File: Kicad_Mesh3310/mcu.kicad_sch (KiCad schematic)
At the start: 41 parts, among them U13 NRF52840-QIAA-R, U4 MX25R1635FZNIH0, X2 S201632M10PF10PPM 32MHz, X4 32.768KHz

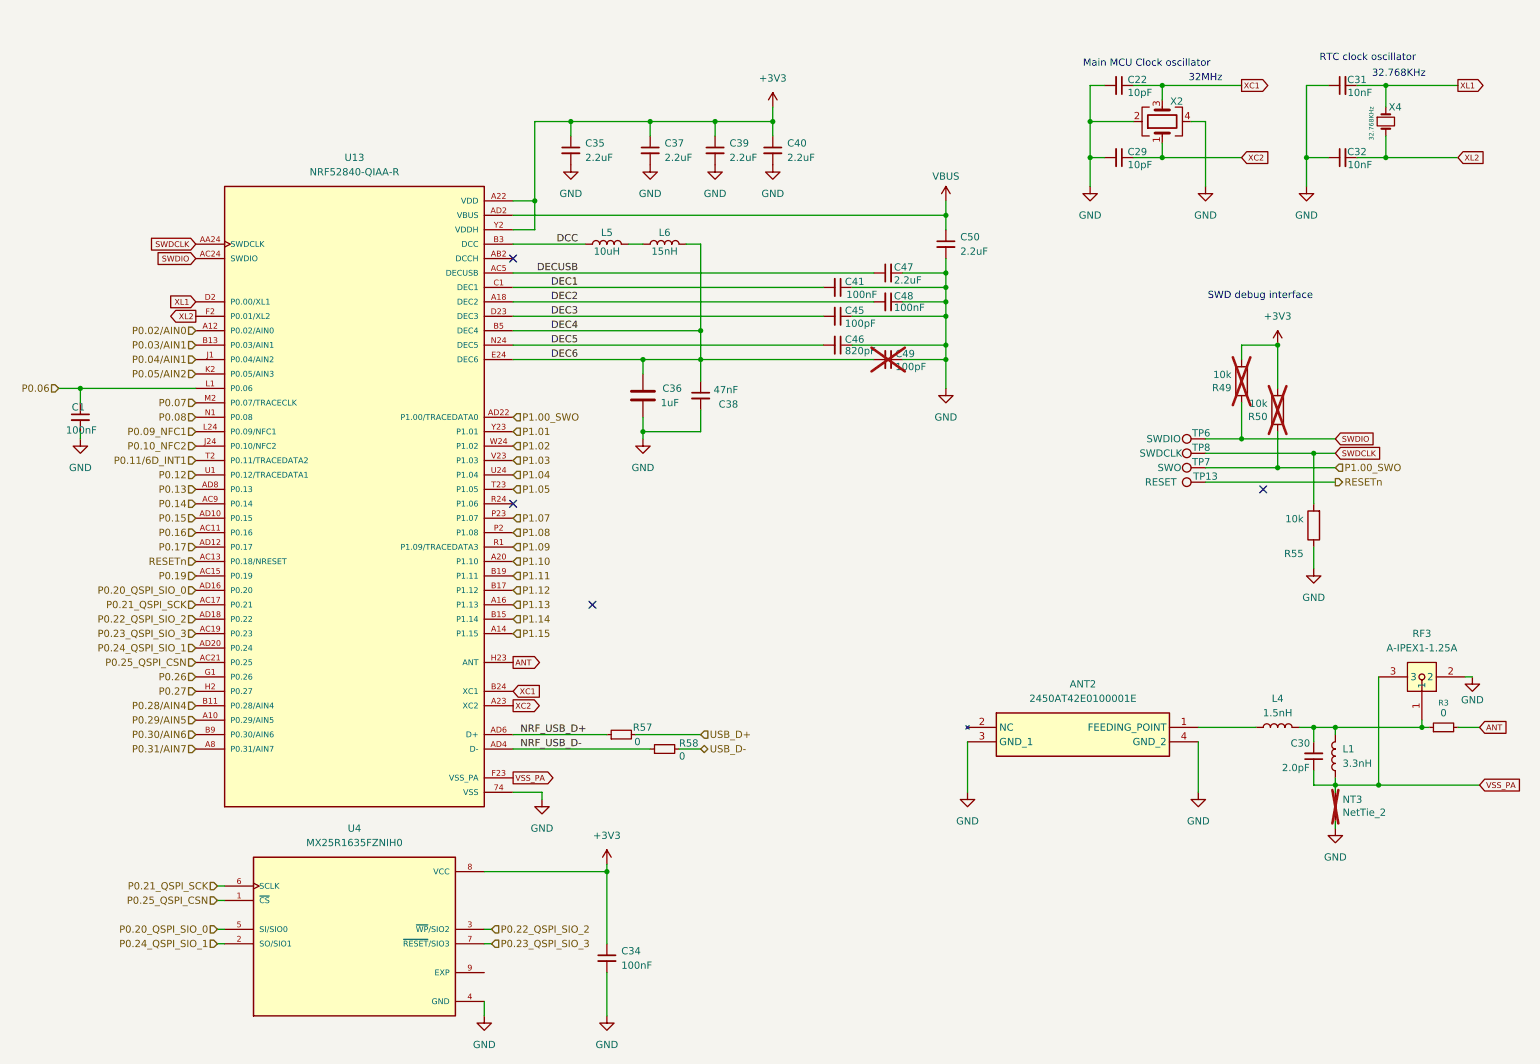
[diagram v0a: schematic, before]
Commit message: shematic changes
small changes in NRF component
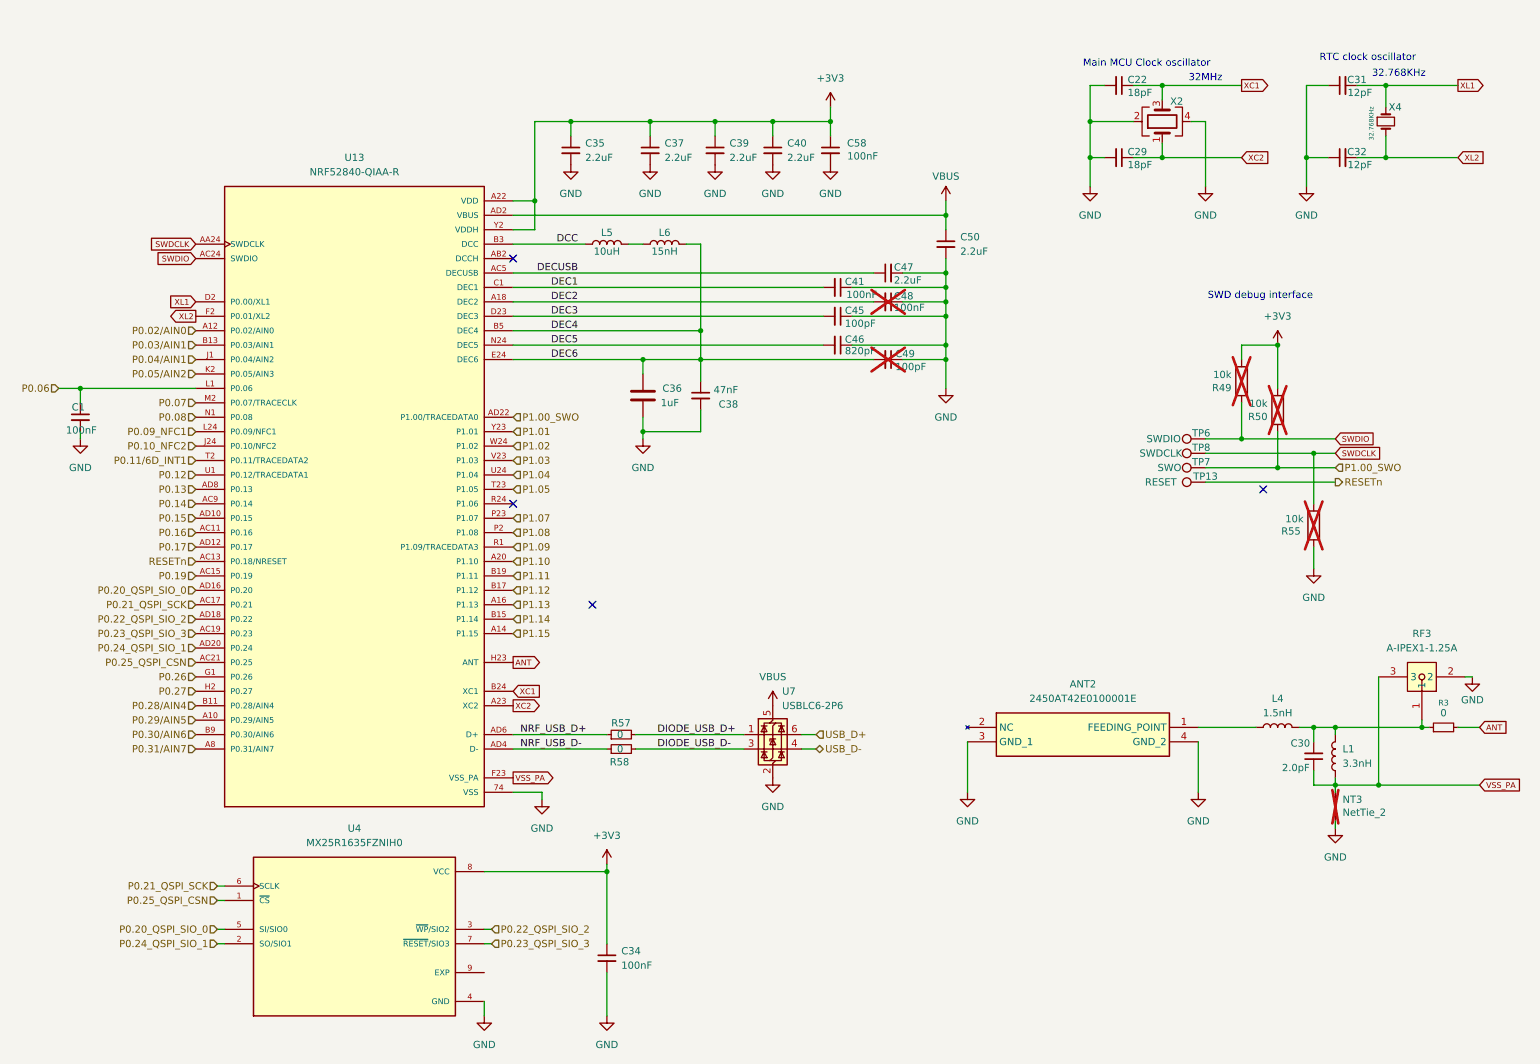
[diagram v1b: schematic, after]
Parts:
- added C58: 100nF, Capacitor_SMD:C_0402_1005Metric, symbol Device:C_Small
- added U7: USBLC6-2P6, Package_TO_SOT_SMD:SOT-666, symbol Power_Protection:USBLC6-2P6
- C22, C29: value 10pF -> 18pF
- C31, C32: value 10nF -> 12pF
- C48, R55: now not fitted
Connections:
- net +3V3: now also C58.1
- net GND: now also C58.2, U7.2 (GND)
- net USB_D+: now also U7.6 (I/O1); no longer R57.2
- net USB_D-: now also U7.4 (I/O2); no longer R58.2
- net VBUS: now also U7.5 (VBUS)
- new net DIODE_USB_D+: R57.2, U7.1 (I/O1)
- new net DIODE_USB_D-: R58.2, U7.3 (I/O2)
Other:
- moved on the sheet: R58

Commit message: Schematic changes
Adding gsm module , interfaces : mic+earspeaker
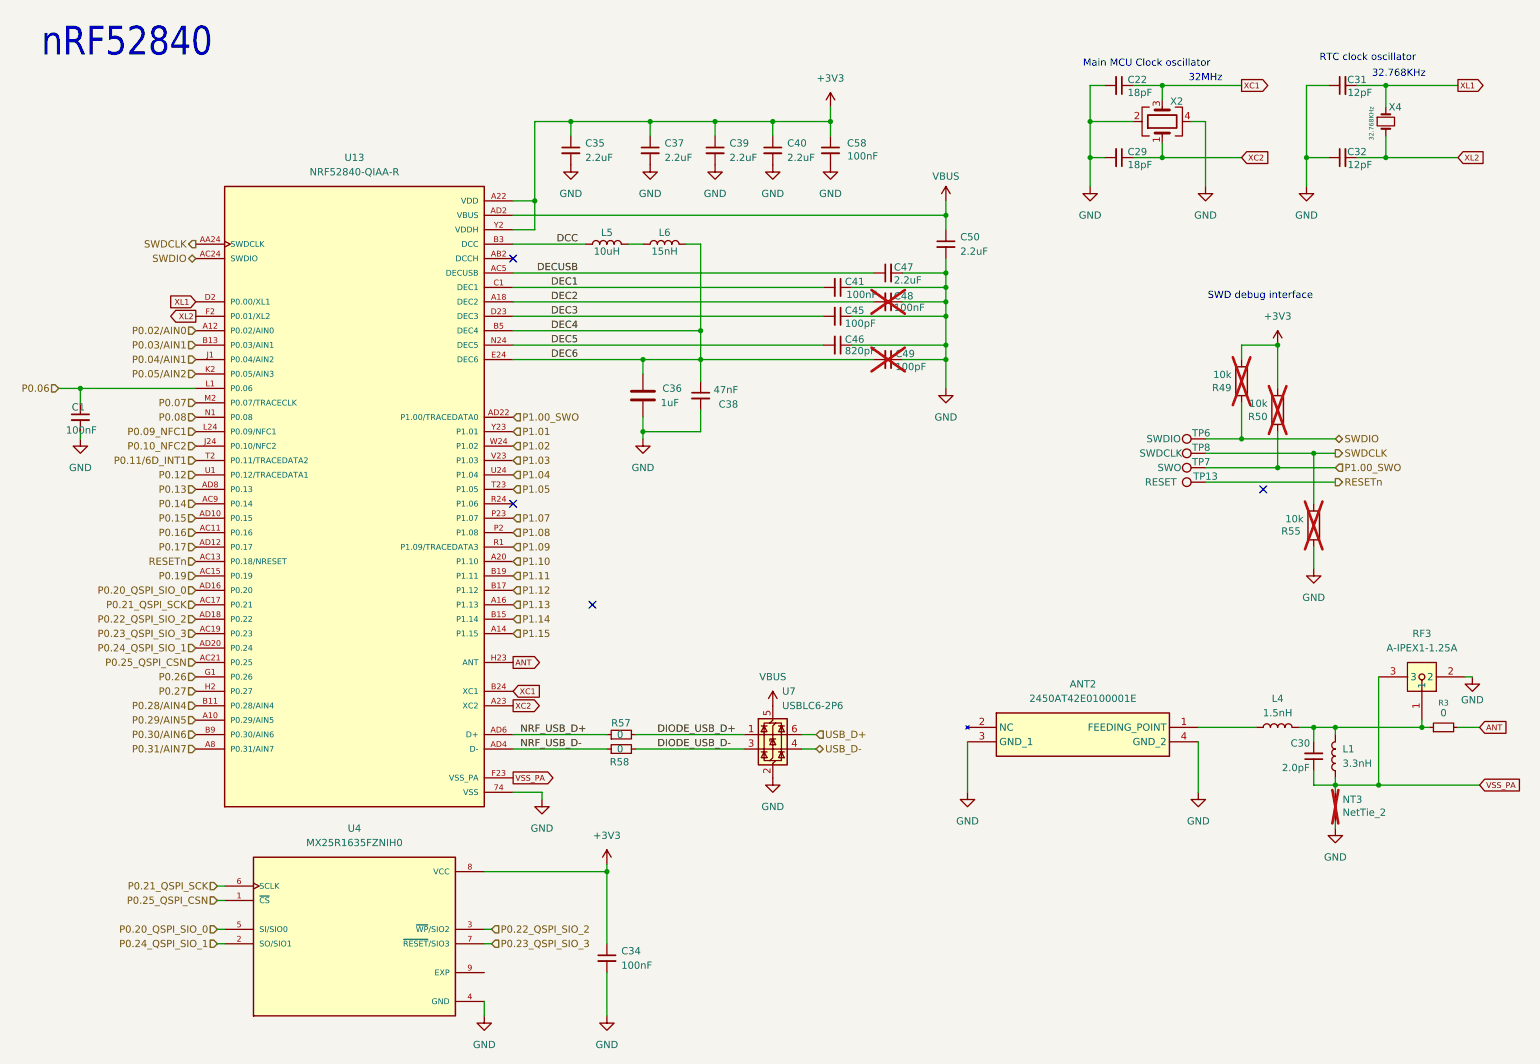
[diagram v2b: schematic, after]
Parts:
- C1: footprint Capacitor_SMD:C_0201_0603Metric -> Resistor_SMD:R_0201_0603Metric
- C58: footprint Capacitor_SMD:C_0402_1005Metric -> Capacitor_SMD:C_0201_0603Metric
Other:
- note added: "nRF52840"
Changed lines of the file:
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@@
 		)
 	)
+	(text "nRF52840"
+		(exclude_from_sim no)
+		(at 18.542 22.098 0)
+		(effects
+			(font
+				(size 5.08 4.318)
+			)
+			(justify left bottom)
+		)
+	)
 	(text "32MHz"
 		(exclude_from_sim no)
@@
 		)
 	)
-	(global_label "SWDCLK"
-		(shape input)
-		(at 246.38 91.44 0)
-		(fields_autoplaced yes)
-		(effects
-			(font
-				(size 1.016 1.016)
-			)
-			(justify left)
-		)
-		(property "Intersheetrefs" "${INTERSHEET_REFS}"
-			(at 254.7671 91.44 0)
-			(effects
-				(font
-					(size 1.27 1.27)
-				)
-				(justify left)
-				(hide yes)
-			)
-		)
-	)
-	(global_label "SWDIO"
-		(shape input)
-		(at 45.72 57.15 180)
-		(fields_autoplaced yes)
-		(effects
-			(font
-				(size 1.016 1.016)
-			)
-			(justify right)
-		)
-		(property "Intersheetrefs" "${INTERSHEET_REFS}"
-			(at 38.6392 57.15 0)
-			(effects
-				(font
-					(size 1.27 1.27)
-				)
-				(justify right)
-				(hide yes)
-			)
-		)
-	)
 	(global_label "XL1"
 		(shape output)
@@
 		)
 	)
-	(global_label "SWDCLK"
-		(shape input)
-		(at 45.72 54.61 180)
-		(fields_autoplaced yes)
-		(effects
-			(font
-				(size 1.016 1.016)
-			)
-			(justify right)
-		)
-		(property "Intersheetrefs" "${INTERSHEET_REFS}"
-			(at 37.3329 54.61 0)
-			(effects
-				(font
-					(size 1.27 1.27)
-				)
-				(justify right)
-				(hide yes)
-			)
-		)
-	)
 	(global_label "XC2"
 		(shape input)
@@
 		)
 	)
-	(global_label "SWDIO"
-		(shape input)
-		(at 246.38 88.9 0)
-		(fields_autoplaced yes)
-		(effects
-			(font
-				(size 1.016 1.016)
-			)
-			(justify left)
-		)
-		(property "Intersheetrefs" "${INTERSHEET_REFS}"
-			(at 253.4608 88.9 0)
-			(effects
-				(font
-					(size 1.27 1.27)
-				)
-				(justify left)
-				(hide yes)
-			)
-		)
-	)
 	(hierarchical_label "P1.07"
 		(shape input)
@@
 		)
 	)
+	(hierarchical_label "SWDIO"
+		(shape bidirectional)
+		(at 246.38 88.9 0)
+		(effects
+			(font
+				(size 1.27 1.27)
+			)
+			(justify left)
+		)
+	)
 	(hierarchical_label "P0.07"
 		(shape input)
@@
 		)
 	)
+	(hierarchical_label "SWDIO"
+		(shape bidirectional)
+		(at 45.72 57.15 180)
+		(effects
+			(font
+				(size 1.27 1.27)
+			)
+			(justify right)
+		)
+	)
 	(hierarchical_label "P1.00_SWO"
 		(shape input)
@@
 		)
 	)
+	(hierarchical_label "SWDCLK"
+		(shape output)
+		(at 45.72 54.61 180)
+		(effects
+			(font
+				(size 1.27 1.27)
+			)
+			(justify right)
+		)
+	)
 	(hierarchical_label "P1.09"
 		(shape input)
@@
 		)
 	)
+	(hierarchical_label "SWDCLK"
+		(shape output)
+		(at 246.38 91.44 0)
+		(effects
+			(font
+				(size 1.27 1.27)
+			)
+			(justify left)
+		)
+	)
 	(hierarchical_label "P0.25_QSPI_CSN"
 		(shape input)
@@
 			)
 		)
-		(property "Footprint" "Capacitor_SMD:C_0402_1005Metric"
+		(property "Footprint" "Capacitor_SMD:C_0201_0603Metric"
 			(at 157.48 38.1 0)
 			(effects
@@
 			)
 		)
-		(property "Footprint" "Capacitor_SMD:C_0201_0603Metric"
+		(property "Footprint" "Resistor_SMD:R_0201_0603Metric"
 			(at 25.4 85.09 0)
 			(effects
